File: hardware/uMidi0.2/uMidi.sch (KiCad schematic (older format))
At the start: 31 parts, among them CON1 USB-MINI-B, IC1 ATXMEGA128A4U-M, IC2 6N138, P1 PDI, P2 MIDI In, P3 MIDI Thru, P4 MIDI T/O, P5 MIDI Out, U1 74LS14

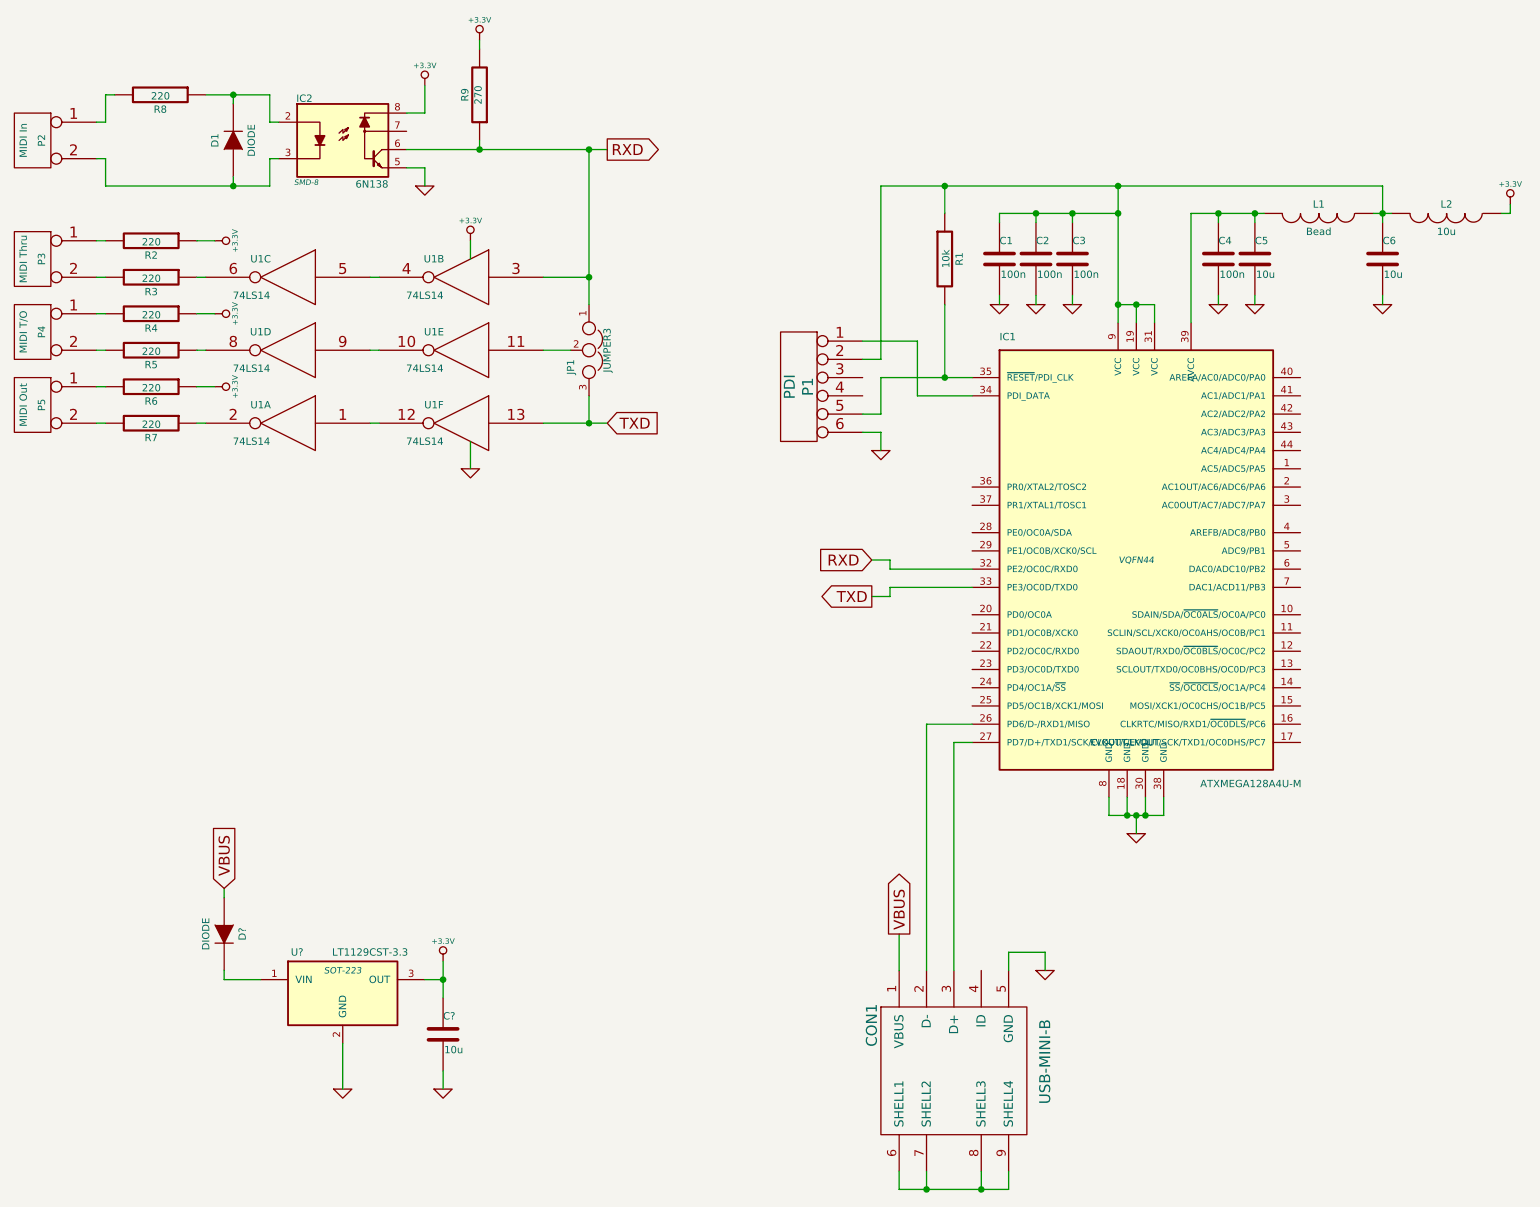
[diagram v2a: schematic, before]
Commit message: Add power input
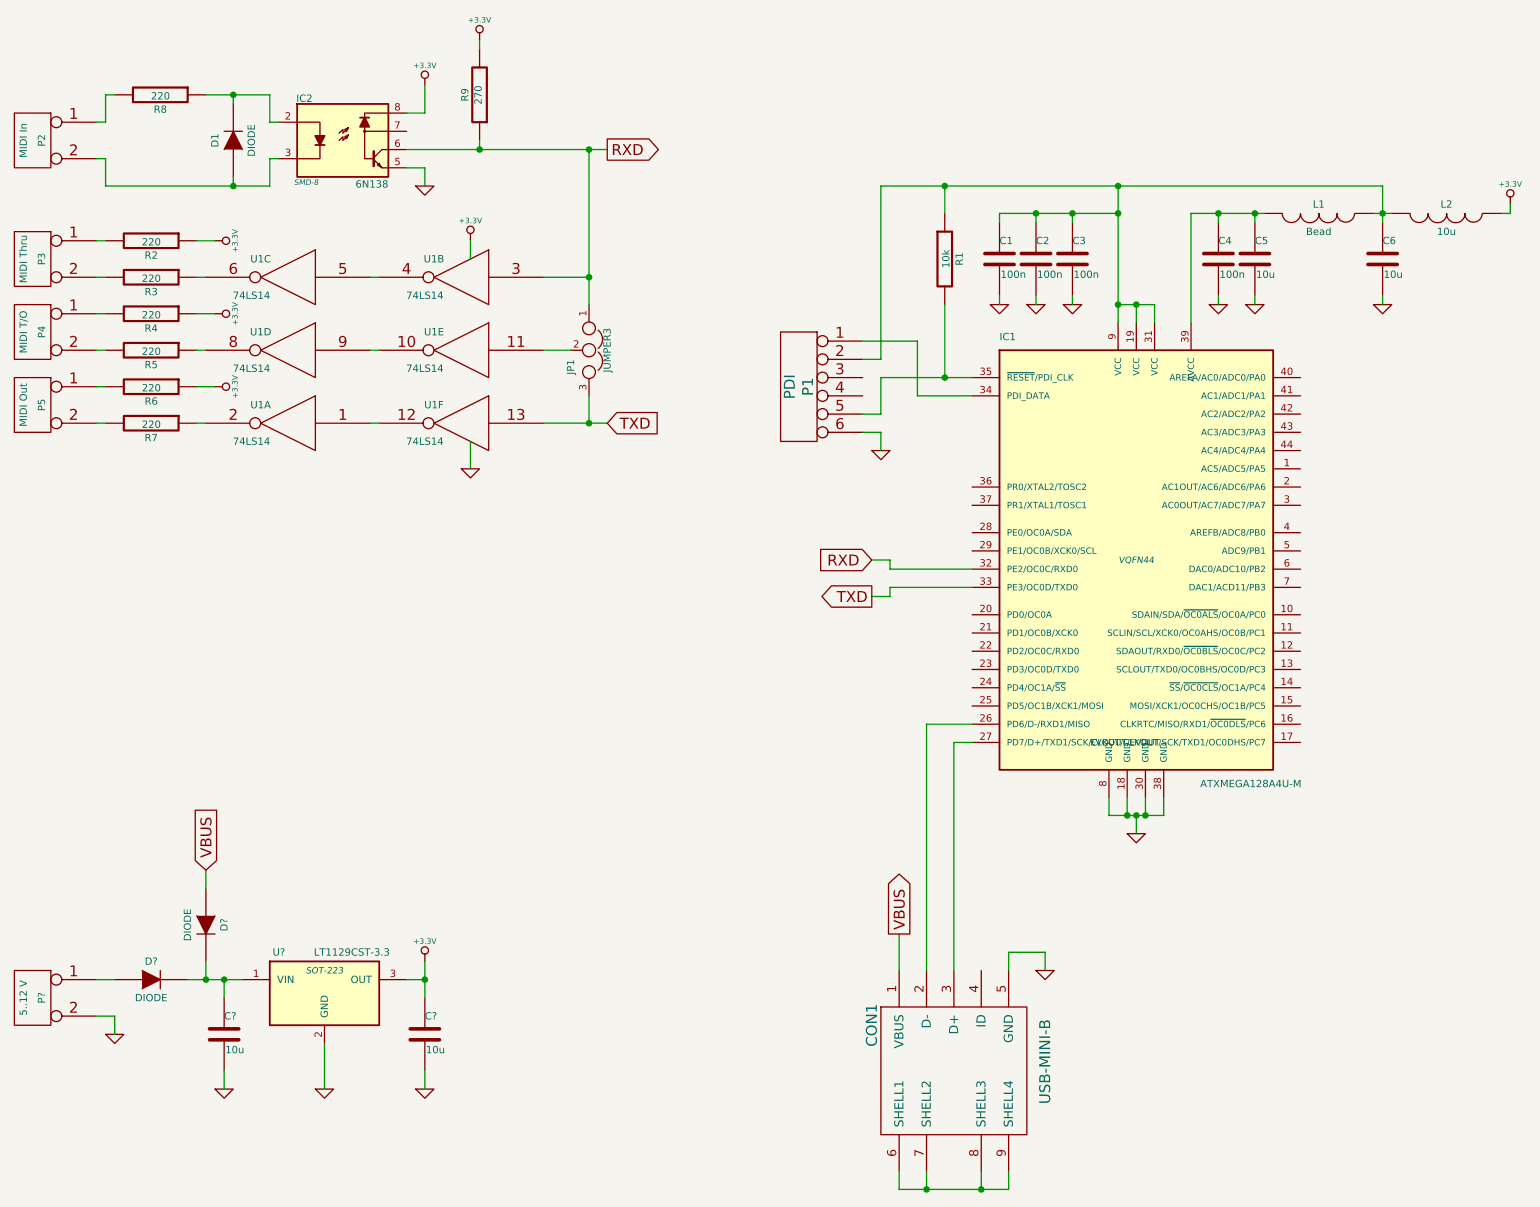
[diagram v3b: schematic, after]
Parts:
- added C?: 10u, symbol C
- added D?: DIODE, symbol DIODE
- added P?: 5..12 V, symbol CONN_2
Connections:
- net GND: now also C?.2, P?.2 (PM)
- net at D?.2 (K), U?.1 (VIN): now also C?.1, D?.2 (K)
- new net: D?.1 (A), P?.1 (P1)
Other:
- moved on the sheet: C?, D?, U?
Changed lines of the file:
@@
 	7200 5150 7200 5250
 Wire Wire Line
-	7050 5150 7150 5150
-Wire Wire Line
-	7150 5150 7200 5150
-Wire Wire Line
-	7200 5150 7250 5150
-Wire Wire Line
-	7250 5150 7350 5150
+	7050 5150 7350 5150
 Wire Wire Line
 	7350 5150 7350 5050
@@
 	7200 2350 7200 2450
 Wire Wire Line
-	7100 2350 7200 2350
-Wire Wire Line
-	7200 2350 7300 2350
+	7100 2350 7300 2350
 Connection ~ 7200 2350
 Wire Wire Line
 	7300 2350 7300 2450
 Wire Wire Line
-	5800 2750 6150 2750
-Wire Wire Line
-	6150 2750 6300 2750
+	5800 2750 6300 2750
 Wire Wire Line
 	6150 2350 6150 2750
@@
 	3550 2100 3550 2000
 Wire Wire Line
-	3950 3000 4200 3000
-Wire Wire Line
-	4200 3000 4300 3000
+	3950 3000 4300 3000
 Wire Wire Line
 	6300 4750 6200 4750
@@
 	5900 7100 5900 7200
 Wire Wire Line
-	5900 7200 6050 7200
-Wire Wire Line
-	6050 7200 6350 7200
-Wire Wire Line
-	6350 7200 6500 7200
+	5900 7200 6500 7200
 Wire Wire Line
 	6500 7200 6500 7100
@@
 Connection ~ 4200 3000
 Wire Wire Line
-	4200 1500 4200 2200
-Wire Wire Line
-	4200 2200 4200 2350
+	4200 1500 4200 2350
 Wire Wire Line
 	4200 2200 3950 2200
@@
 $EndComp
 Wire Wire Line
-	1550 1700 2250 1700
-Wire Wire Line
-	2250 1700 2450 1700
+	1550 1700 2450 1700
 Wire Wire Line
 	2450 1700 2450 1550
@@
 Connection ~ 2250 1700
 Wire Wire Line
-	2100 1200 2250 1200
-Wire Wire Line
-	2250 1200 2450 1200
+	2100 1200 2450 1200
 Wire Wire Line
 	2450 1200 2450 1350
@@
 $EndComp
 Wire Wire Line
-	3200 1500 3600 1500
-Wire Wire Line
-	3600 1500 4200 1500
-Wire Wire Line
-	4200 1500 4300 1500
+	3200 1500 4300 1500
 Wire Wire Line
 	3600 1500 3600 1450
@@
 	7500 1850 7500 2450
 Wire Wire Line
-	7500 1850 7650 1850
-Wire Wire Line
-	7650 1850 7850 1850
-Wire Wire Line
-	7850 1850 7900 1850
+	7500 1850 7900 1850
 Wire Wire Line
 	7850 1900 7850 1850
@@
 $EndComp
 Wire Wire Line
-	6450 1850 6650 1850
-Wire Wire Line
-	6650 1850 6850 1850
-Wire Wire Line
-	6850 1850 7100 1850
-Wire Wire Line
-	7100 1700 7100 1850
-Wire Wire Line
-	7100 1850 7100 2350
-Wire Wire Line
-	7100 2350 7100 2450
+	6450 1850 7100 1850
+Wire Wire Line
+	7100 1700 7100 2450
 Wire Wire Line
 	6850 2350 6850 2300
@@
 	9250 1850 9250 1800
 Wire Wire Line
-	8500 1850 8550 1850
-Wire Wire Line
-	8550 1850 8600 1850
-Wire Wire Line
-	8550 1700 8550 1850
-Wire Wire Line
-	8550 1850 8550 1900
+	8500 1850 8600 1850
+Wire Wire Line
+	8550 1700 8550 1900
 Connection ~ 8550 1850
 Wire Wire Line
-	5800 1700 6150 1700
-Wire Wire Line
-	6150 1700 7100 1700
-Wire Wire Line
-	7100 1700 8550 1700
+	5800 1700 8550 1700
 Wire Wire Line
 	6150 1700 6150 1850
@@
 L LT1129CST-3.3 U?
 U 1 1 53CAB726
-P 2850 6100
-F 0 "U?" H 2600 6300 40  0000 C CNN
-F 1 "LT1129CST-3.3" H 3000 6300 40  0000 C CNN
-F 2 "SOT-223" H 2850 6200 35  0000 C CIN
-F 3 "" H 2850 6100 60  0000 C CNN
-	1    2850 6100
+P 2750 6100
+F 0 "U?" H 2500 6300 40  0000 C CNN
+F 1 "LT1129CST-3.3" H 2900 6300 40  0000 C CNN
+F 2 "SOT-223" H 2750 6200 35  0000 C CIN
+F 3 "" H 2750 6100 60  0000 C CNN
+	1    2750 6100
 	1    0    0    -1
 $EndComp
 Text GLabel 5900 5800 1    60   Output ~ 0
 VBUS
-Text GLabel 2200 5550 1    60   Input ~ 0
+Text GLabel 2100 5450 1    60   Input ~ 0
 VBUS
 $Comp
 L DIODE D?
 U 1 1 53CAB822
-P 2200 5800
-F 0 "D?" H 2200 5900 40  0000 C CNN
-F 1 "DIODE" H 2200 5700 40  0000 C CNN
-F 2 "" H 2200 5800 60  0000 C CNN
-F 3 "" H 2200 5800 60  0000 C CNN
-	1    2200 5800
-	0    1    1    0
-$EndComp
-Wire Wire Line
-	2200 5600 2200 5550
-Wire Wire Line
-	2200 6000 2200 6050
-Wire Wire Line
-	2200 6050 2400 6050
+P 2100 5750
+F 0 "D?" H 2100 5850 40  0000 C CNN
+F 1 "DIODE" H 2100 5650 40  0000 C CNN
+F 2 "" H 2100 5750 60  0000 C CNN
+F 3 "" H 2100 5750 60  0000 C CNN
+	1    2100 5750
+	0    1    1    0
+$EndComp
+Wire Wire Line
+	2100 5550 2100 5450
+Wire Wire Line
+	2100 5950 2100 6050
+Wire Wire Line
+	2000 6050 2300 6050
 $Comp
 L GND #PWR?
 U 1 1 53CAB9F8
-P 2850 6650
-F 0 "#PWR?" H 2850 6650 30  0001 C CNN
-F 1 "GND" H 2850 6580 30  0001 C CNN
-F 2 "" H 2850 6650 60  0000 C CNN
-F 3 "" H 2850 6650 60  0000 C CNN
-	1    2850 6650
-	1    0    0    -1
-$EndComp
-Wire Wire Line
-	2850 6650 2850 6400
+P 2750 6650
+F 0 "#PWR?" H 2750 6650 30  0001 C CNN
+F 1 "GND" H 2750 6580 30  0001 C CNN
+F 2 "" H 2750 6650 60  0000 C CNN
+F 3 "" H 2750 6650 60  0000 C CNN
+	1    2750 6650
+	1    0    0    -1
+$EndComp
+Wire Wire Line
+	2750 6650 2750 6400
 $Comp
 L C C?
 U 1 1 53CABAC9
-P 3400 6350
-F 0 "C?" H 3400 6450 40  0000 L CNN
-F 1 "10u" H 3406 6265 40  0000 L CNN
-F 2 "" H 3438 6200 30  0000 C CNN
-F 3 "" H 3400 6350 60  0000 C CNN
-	1    3400 6350
+P 3300 6350
+F 0 "C?" H 3300 6450 40  0000 L CNN
+F 1 "10u" H 3306 6265 40  0000 L CNN
+F 2 "" H 3338 6200 30  0000 C CNN
+F 3 "" H 3300 6350 60  0000 C CNN
+	1    3300 6350
 	1    0    0    -1
 $EndComp
@@
 L GND #PWR?
 U 1 1 53CABAD4
-P 3400 6650
-F 0 "#PWR?" H 3400 6650 30  0001 C CNN
-F 1 "GND" H 3400 6580 30  0001 C CNN
-F 2 "" H 3400 6650 60  0000 C CNN
-F 3 "" H 3400 6650 60  0000 C CNN
-	1    3400 6650
-	1    0    0    -1
-$EndComp
-Wire Wire Line
-	3400 6650 3400 6550
-Wire Wire Line
-	3400 5950 3400 6050
-Wire Wire Line
-	3400 6050 3400 6150
-Wire Wire Line
-	3400 6050 3300 6050
+P 3300 6650
+F 0 "#PWR?" H 3300 6650 30  0001 C CNN
+F 1 "GND" H 3300 6580 30  0001 C CNN
+F 2 "" H 3300 6650 60  0000 C CNN
+F 3 "" H 3300 6650 60  0000 C CNN
+	1    3300 6650
+	1    0    0    -1
+$EndComp
+Wire Wire Line
+	3300 6650 3300 6550
+Wire Wire Line
+	3300 5950 3300 6150
+Wire Wire Line
+	3300 6050 3200 6050
 $Comp
 L +3.3V #PWR?
 U 1 1 53CABBFC
-P 3400 5950
-F 0 "#PWR?" H 3400 5910 30  0001 C CNN
-F 1 "+3.3V" H 3400 6060 30  0000 C CNN
-F 2 "" H 3400 5950 60  0000 C CNN
-F 3 "" H 3400 5950 60  0000 C CNN
-	1    3400 5950
-	1    0    0    -1
-$EndComp
-Connection ~ 3400 6050
+P 3300 5950
+F 0 "#PWR?" H 3300 5910 30  0001 C CNN
+F 1 "+3.3V" H 3300 6060 30  0000 C CNN
+F 2 "" H 3300 5950 60  0000 C CNN
+F 3 "" H 3300 5950 60  0000 C CNN
+	1    3300 5950
+	1    0    0    -1
+$EndComp
+Connection ~ 3300 6050
+$Comp
+L C C?
+U 1 1 53CAA38D
+P 2200 6350
+F 0 "C?" H 2200 6450 40  0000 L CNN
+F 1 "10u" H 2206 6265 40  0000 L CNN
+F 2 "" H 2238 6200 30  0000 C CNN
+F 3 "" H 2200 6350 60  0000 C CNN
+	1    2200 6350
+	1    0    0    -1
+$EndComp
+Wire Wire Line
+	2200 6050 2200 6150
+Connection ~ 2200 6050
+$Comp
+L GND #PWR?
+U 1 1 53CAA437
+P 2200 6650
+F 0 "#PWR?" H 2200 6650 30  0001 C CNN
+F 1 "GND" H 2200 6580 30  0001 C CNN
+F 2 "" H 2200 6650 60  0000 C CNN
+F 3 "" H 2200 6650 60  0000 C CNN
+	1    2200 6650
+	1    0    0    -1
+$EndComp
+Wire Wire Line
+	2200 6650 2200 6550
+$Comp
+L DIODE D?
+U 1 1 53CAA4CA
+P 1800 6050
+F 0 "D?" H 1800 6150 40  0000 C CNN
+F 1 "DIODE" H 1800 5950 40  0000 C CNN
+F 2 "" H 1800 6050 60  0000 C CNN
+F 3 "" H 1800 6050 60  0000 C CNN
+	1    1800 6050
+	1    0    0    -1
+$EndComp
+Connection ~ 2100 6050
+$Comp
+L CONN_2 P?
+U 1 1 53CAA6B4
+P 1150 6150
+F 0 "P?" V 1100 6150 40  0000 C CNN
+F 1 "5..12 V" V 1200 6150 40  0000 C CNN
+F 2 "" H 1150 6150 60  0000 C CNN
+F 3 "" H 1150 6150 60  0000 C CNN
+	1    1150 6150
+	-1   0    0    -1
+$EndComp
+Wire Wire Line
+	1500 6050 1600 6050
+$Comp
+L GND #PWR?
+U 1 1 53CAA74E
+P 1600 6350
+F 0 "#PWR?" H 1600 6350 30  0001 C CNN
+F 1 "GND" H 1600 6280 30  0001 C CNN
+F 2 "" H 1600 6350 60  0000 C CNN
+F 3 "" H 1600 6350 60  0000 C CNN
+	1    1600 6350
+	1    0    0    -1
+$EndComp
+Wire Wire Line
+	1600 6350 1600 6250
+Wire Wire Line
+	1600 6250 1500 6250
 $EndSCHEMATC

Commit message: Add decoupling caps to midi circuit
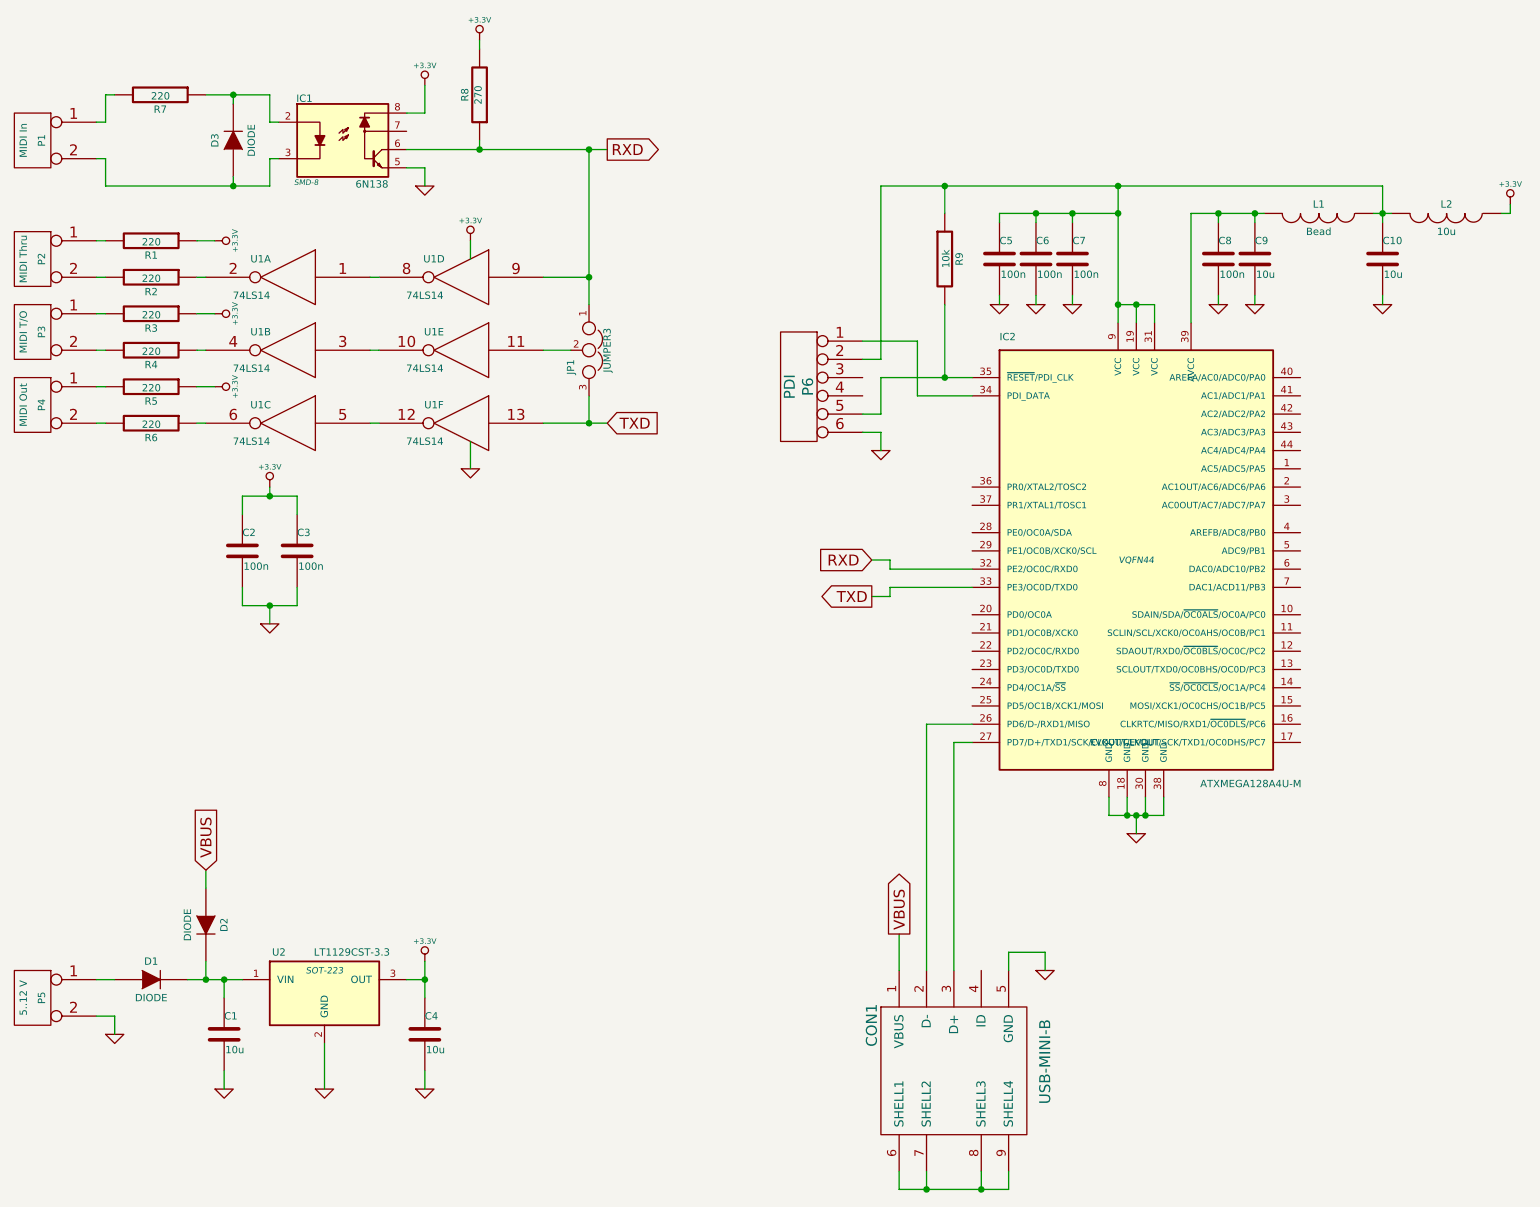
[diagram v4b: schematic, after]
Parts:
- added C2, C3: 100n, symbol C
- gave numbers to parts that had none: 6
- renumbered C6 to C10, C1 to C5, C2 to C6, C3 to C7, C4 to C8, C5 to C9, D1 to D3, IC2 to IC1, IC1 to IC2, P2 to P1, P3 to P2, P4 to P3, P5 to P4, P1 to P6, R2 to R1, R3 to R2, R4 to R3, R5 to R4, R6 to R5, R7 to R6, R8 to R7, R9 to R8, R1 to R9
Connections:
- net +3.3V: now also C2.1, C3.1
- net GND: now also C2.2, C3.2
- net RXD: now also U1.9; no longer U1.3
- net at R2.1: now also U1.2; no longer U1.6
- net at R4.1: now also U1.4; no longer U1.8
- net at U1.10: now also U1.3; no longer U1.9
- net at U1.12: now also U1.5; no longer U1.1
- net at R6.1: now also U1.6; no longer U1.2
- new net: U1.1, U1.8
